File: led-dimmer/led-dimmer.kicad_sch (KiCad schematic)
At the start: 14 parts, among them J1 Screw_Terminal_01x02, J2 Screw_Terminal_01x02, Q1 IRLML6344, U1 LM555xM

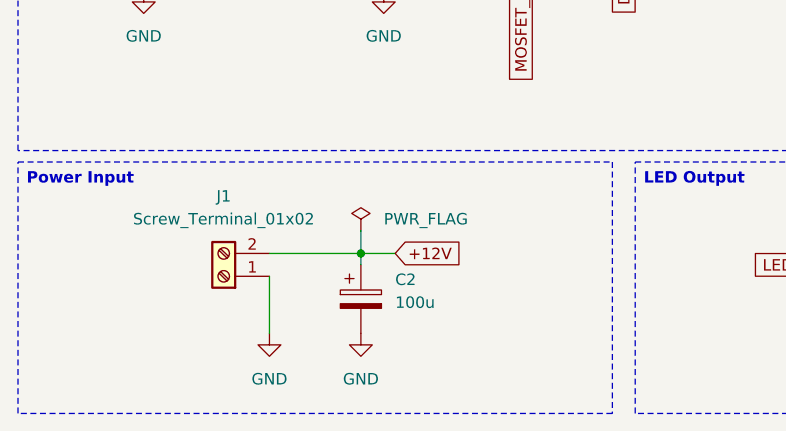
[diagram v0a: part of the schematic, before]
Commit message: Updated LED Schematic and PCB
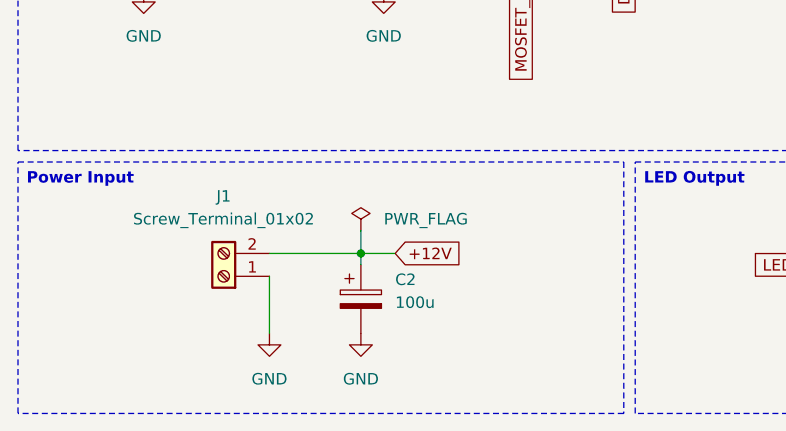
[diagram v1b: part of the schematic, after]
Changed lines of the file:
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@@
 	(title_block
 		(title "LED Dimmer Schematic")
-		(date "2026-06-28")
+		(date "2026-07-20")
 		(rev "1.0")
 	)
@@
 		(exclude_from_sim no)
 		(at 16.51 77.47 0)
-		(size 66.04 27.94)
+		(size 67.31 27.94)
 		(margins 0.9525 0.9525 0.9525 0.9525)
 		(stroke

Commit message: Updated output connectors and slimmed LED Dimmer PCB
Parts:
- removed J1, J2: Screw_Terminal_01x02, TerminalBlock:TerminalBlock_MaiXu_MX126-5.0-02P_1x02_P5.00mm, symbol Connector:Screw_Terminal_01x02
- added J1, J2: Conn_01x02_Pin, Connector_JST:JST_PH_B2B-PH-K_1x02_P2.00mm_Vertical, symbol Connector:Conn_01x02_Pin
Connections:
- net +12V: now also J1.1 (Pin_1), J2.1 (Pin_1)
- net GND: now also J1.2 (Pin_2)
- net LED_PWM: now also J2.2 (Pin_2)
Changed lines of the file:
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@@
 	(title_block
 		(title "LED Dimmer Schematic")
-		(date "2026-07-20")
+		(date "2026-07-25")
 		(rev "1.0")
 	)
@@
 				(path "/97f4d0d2-49dd-4867-ad6b-0ece5467e23e"
 					(reference "R2")
+					(unit 1)
+				)
+			)
+		)
+	)
+	(symbol
+		(lib_id "Connector:Conn_01x02_Pin")
+		(at 114.3 91.44 180)
+		(unit 1)
+		(body_style 1)
+		(exclude_from_sim no)
+		(in_bom yes)
+		(on_board yes)
+		(in_pos_files yes)
+		(dnp no)
+		(fields_autoplaced yes)
+		(property "Reference" "J2"
+			(at 115.57 88.8999 0)
+			(show_name no)
+			(do_not_autoplace no)
+			(effects
+				(font
+					(size 1.27 1.27)
+				)
+				(justify right)
+			)
+		)
+		(property "Value" "Conn_01x02_Pin"
+			(at 115.57 91.4399 0)
+			(show_name no)
+			(do_not_autoplace no)
+			(effects
+				(font
+					(size 1.27 1.27)
+				)
+				(justify right)
+			)
+		)
+		(property "Footprint" "Connector_JST:JST_PH_B2B-PH-K_1x02_P2.00mm_Vertical"
+			(at 114.3 91.44 0)
+			(hide yes)
+			(show_name no)
+			(do_not_autoplace no)
+			(effects
+				(font
+					(size 1.27 1.27)
+				)
+			)
+		)
+		(property "Datasheet" ""
+			(at 114.3 91.44 0)
+			(hide yes)
+			(show_name no)
+			(do_not_autoplace no)
+			(effects
+				(font
+					(size 1.27 1.27)
+				)
+			)
+		)
+		(property "Description" "Generic connector, single row, 01x02, script generated"
+			(at 114.3 91.44 0)
+			(hide yes)
+			(show_name no)
+			(do_not_autoplace no)
+			(effects
+				(font
+					(size 1.27 1.27)
+				)
+			)
+		)
+		(pin "1"
+		)
+		(pin "2"
+		)
+		(instances
+			(project "led-dimmer"
+				(path "/97f4d0d2-49dd-4867-ad6b-0ece5467e23e"
+					(reference "J2")
 					(unit 1)
 				)
@@
 				(path "/97f4d0d2-49dd-4867-ad6b-0ece5467e23e"
 					(reference "#PWR02")
-					(unit 1)
-				)
-			)
-		)
-	)
-	(symbol
-		(lib_id "Connector:Screw_Terminal_01x02")
-		(at 39.37 90.17 180)
-		(unit 1)
-		(body_style 1)
-		(exclude_from_sim no)
-		(in_bom yes)
-		(on_board yes)
-		(in_pos_files yes)
-		(dnp no)
-		(fields_autoplaced yes)
-		(property "Reference" "J1"
-			(at 39.37 81.28 0)
-			(show_name no)
-			(do_not_autoplace no)
-			(effects
-				(font
-					(size 1.27 1.27)
-				)
-			)
-		)
-		(property "Value" "Screw_Terminal_01x02"
-			(at 39.37 83.82 0)
-			(show_name no)
-			(do_not_autoplace no)
-			(effects
-				(font
-					(size 1.27 1.27)
-				)
-			)
-		)
-		(property "Footprint" "TerminalBlock:TerminalBlock_MaiXu_MX126-5.0-02P_1x02_P5.00mm"
-			(at 39.37 90.17 0)
-			(hide yes)
-			(show_name no)
-			(do_not_autoplace no)
-			(effects
-				(font
-					(size 1.27 1.27)
-				)
-			)
-		)
-		(property "Datasheet" ""
-			(at 39.37 90.17 0)
-			(hide yes)
-			(show_name no)
-			(do_not_autoplace no)
-			(effects
-				(font
-					(size 1.27 1.27)
-				)
-			)
-		)
-		(property "Description" "Generic screw terminal, single row, 01x02, script generated (kicad-library-utils/schlib/autogen/connector/)"
-			(at 39.37 90.17 0)
-			(hide yes)
-			(show_name no)
-			(do_not_autoplace no)
-			(effects
-				(font
-					(size 1.27 1.27)
-				)
-			)
-		)
-		(pin "1"
-		)
-		(pin "2"
-		)
-		(instances
-			(project "led-dimmer"
-				(path "/97f4d0d2-49dd-4867-ad6b-0ece5467e23e"
-					(reference "J1")
 					(unit 1)
 				)
@@
 	)
 	(symbol
-		(lib_id "Connector:Screw_Terminal_01x02")
-		(at 114.3 88.9 0)
-		(unit 1)
-		(body_style 1)
-		(exclude_from_sim no)
-		(in_bom yes)
-		(on_board yes)
-		(in_pos_files yes)
-		(dnp no)
-		(fields_autoplaced yes)
-		(property "Reference" "J2"
-			(at 116.84 88.8999 0)
-			(show_name no)
-			(do_not_autoplace no)
-			(effects
-				(font
-					(size 1.27 1.27)
-				)
-				(justify left)
-			)
-		)
-		(property "Value" "Screw_Terminal_01x02"
-			(at 116.84 91.4399 0)
-			(show_name no)
-			(do_not_autoplace no)
-			(effects
-				(font
-					(size 1.27 1.27)
-				)
-				(justify left)
-			)
-		)
-		(property "Footprint" "TerminalBlock:TerminalBlock_MaiXu_MX126-5.0-02P_1x02_P5.00mm"
-			(at 114.3 88.9 0)
-			(hide yes)
-			(show_name no)
-			(do_not_autoplace no)
-			(effects
-				(font
-					(size 1.27 1.27)
-				)
-			)
-		)
-		(property "Datasheet" ""
-			(at 114.3 88.9 0)
-			(hide yes)
-			(show_name no)
-			(do_not_autoplace no)
-			(effects
-				(font
-					(size 1.27 1.27)
-				)
-			)
-		)
-		(property "Description" "Generic screw terminal, single row, 01x02, script generated (kicad-library-utils/schlib/autogen/connector/)"
-			(at 114.3 88.9 0)
-			(hide yes)
-			(show_name no)
-			(do_not_autoplace no)
-			(effects
-				(font
-					(size 1.27 1.27)
-				)
-			)
-		)
-		(pin "1"
-		)
-		(pin "2"
-		)
-		(instances
-			(project "led-dimmer"
-				(path "/97f4d0d2-49dd-4867-ad6b-0ece5467e23e"
-					(reference "J2")
-					(unit 1)
-				)
-			)
-		)
-	)
-	(symbol
 		(lib_id "Device:C")
 		(at 48.26 33.02 90)
@@
 					(unit 1)
 				)
+			)
+		)
+	)
+	(symbol
+		(lib_id "Connector:Conn_01x02_Pin")
+		(at 39.37 87.63 0)
+		(unit 1)
+		(body_style 1)
+		(exclude_from_sim no)
+		(in_bom yes)
+		(on_board yes)
+		(in_pos_files yes)
+		(dnp no)
+		(fields_autoplaced yes)
+		(property "Reference" "J1"
+			(at 40.005 82.55 0)
+			(show_name no)
+			(do_not_autoplace no)
+			(effects
+				(font
+					(size 1.27 1.27)
+				)
+			)
+		)
+		(property "Value" "Conn_01x02_Pin"
+			(at 40.005 85.09 0)
+			(show_name no)
+			(do_not_autoplace no)
+			(effects
+				(font
+					(size 1.27 1.27)
+				)
+			)
+		)
+		(property "Footprint" "Connector_JST:JST_PH_B2B-PH-K_1x02_P2.00mm_Vertical"
+			(at 39.37 87.63 0)
+			(hide yes)
+			(show_name no)
+			(do_not_autoplace no)
+			(effects
+				(font
+					(size 1.27 1.27)
+				)
+			)
+		)
+		(property "Datasheet" ""
+			(at 39.37 87.63 0)
+			(hide yes)
+			(show_name no)
+			(do_not_autoplace no)
+			(effects
+				(font
+					(size 1.27 1.27)
+				)
+			)
+		)
+		(property "Description" "Generic connector, single row, 01x02, script generated"
+			(at 39.37 87.63 0)
+			(hide yes)
+			(show_name no)
+			(do_not_autoplace no)
+			(effects
+				(font
+					(size 1.27 1.27)
+				)
+			)
+		)
+		(pin "1"
+		)
+		(pin "2"
+		)
+		(instances
+			(project "led-dimmer"
+				(path "/97f4d0d2-49dd-4867-ad6b-0ece5467e23e"
+					(reference "J1")
+					(unit 1)
+				)

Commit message: Update LED dimmer PCB for revised components
- Switch power and LED connections to JST B2B-XH-A connectors
- Update bulk capacitor to 470uF
- Change NE555 to DIP-8 package
- Increase PCB size and revise component placement/routing
- Update schematic reference designators
- Refresh README component and design documentation
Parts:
- removed U1: LM555xM, Package_SO:SOIC-8_3.9x4.9mm_P1.27mm, symbol Timer:LM555xM
- added U1: NE555P, Package_DIP:DIP-8_W7.62mm, symbol Timer:NE555P
- C3: renamed from C2; value 100u -> 470u; footprint Capacitor_THT:CP_Radial_D5.0mm_P2.50mm -> Capacitor_THT:CP_Radial_D6.3mm_P2.50mm
- J1, J2: footprint Connector_JST:JST_PH_B2B-PH-K_1x02_P2.00mm_Vertical -> footprints:JST_B2B-XH-A
- renumbered C3 to C2
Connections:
- net +12V: now also U1.4 (~{RST}), U1.8 (VCC)
- net DISCHARGE: now also U1.7 (DISCH)
- net GND: now also U1.1 (GND)
- net TIMING: now also U1.2 (TRIG), U1.6 (THRES)
- net at R2.2: now also U1.3 (OUT)
- net at C2.2: now also U1.5 (CONT)
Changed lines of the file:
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@@
 	(title_block
 		(title "LED Dimmer Schematic")
-		(date "2026-07-25")
-		(rev "1.0")
+		(date "2026-08-15")
+		(rev "1.1")
 	)
 	(text_box "Power Input"
@@
 	)
 	(junction
-		(at 57.15 55.88)
-		(diameter 0)
-		(color 0 0 0 0)
-	)
-	(junction
 		(at 124.46 44.45)
 		(diameter 0)
@@
 	(junction
 		(at 35.56 43.18)
+		(diameter 0)
+		(color 0 0 0 0)
+	)
+	(junction
+		(at 57.15 55.88)
 		(diameter 0)
 		(color 0 0 0 0)
@@
 			)
 		)
-		(property "Footprint" "Connector_JST:JST_PH_B2B-PH-K_1x02_P2.00mm_Vertical"
+		(property "Footprint" "footprints:JST_B2B-XH-A"
 			(at 114.3 91.44 0)
 			(hide yes)
@@
 		(in_pos_files yes)
 		(dnp no)
-		(property "Reference" "C2"
+		(property "Reference" "C3"
 			(at 58.42 90.5509 0)
 			(show_name no)
@@
 			)
 		)
-		(property "Value" "100u"
+		(property "Value" "470u"
 			(at 58.42 93.0909 0)
 			(show_name no)
@@
 			)
 		)
-		(property "Footprint" "Capacitor_THT:CP_Radial_D5.0mm_P2.50mm"
+		(property "Footprint" "Capacitor_THT:CP_Radial_D6.3mm_P2.50mm"
 			(at 55.5752 96.52 0)
 			(hide yes)
@@
 			(project "led-dimmer"
 				(path "/97f4d0d2-49dd-4867-ad6b-0ece5467e23e"
-					(reference "C2")
+					(reference "C3")
 					(unit 1)
 				)
@@
 		(dnp no)
 		(fields_autoplaced yes)
-		(property "Reference" "#PWR04"
+		(property "Reference" "#PWR03"
 			(at 44.45 102.87 0)
 			(hide yes)
@@
 			(project "led-dimmer"
 				(path "/97f4d0d2-49dd-4867-ad6b-0ece5467e23e"
-					(reference "#PWR04")
+					(reference "#PWR03")
 					(unit 1)
 				)
@@
 		(dnp no)
 		(fields_autoplaced yes)
-		(property "Reference" "#PWR02"
+		(property "Reference" "#PWR04"
 			(at 54.61 102.87 0)
 			(hide yes)
@@
 			(project "led-dimmer"
 				(path "/97f4d0d2-49dd-4867-ad6b-0ece5467e23e"
-					(reference "#PWR02")
+					(reference "#PWR04")
 					(unit 1)
 				)
@@
 		(dnp no)
 		(fields_autoplaced yes)
-		(property "Reference" "#PWR03"
+		(property "Reference" "#PWR02"
 			(at 40.64 41.91 0)
 			(hide yes)
@@
 			(project "led-dimmer"
 				(path "/97f4d0d2-49dd-4867-ad6b-0ece5467e23e"
-					(reference "#PWR03")
+					(reference "#PWR02")
 					(unit 1)
 				)
@@
 	)
 	(symbol
-		(lib_name "LM555xM_1")
-		(lib_id "Timer:LM555xM")
+		(lib_id "Timer:NE555P")
 		(at 57.15 45.72 0)
 		(unit 1)
@@
 		(in_pos_files yes)
 		(dnp no)
+		(fields_autoplaced yes)
 		(property "Reference" "U1"
-			(at 64.77 34.29 0)
-			(show_name no)
-			(do_not_autoplace no)
-			(effects
-				(font
-					(size 1.27 1.27)
-				)
-			)
-		)
-		(property "Value" "LM555xM"
-			(at 64.77 36.83 0)
-			(show_name no)
-			(do_not_autoplace no)
-			(effects
-				(font
-					(size 1.27 1.27)
-				)
-			)
-		)
-		(property "Footprint" "Package_SO:SOIC-8_3.9x4.9mm_P1.27mm"
+			(at 69.85 39.2998 0)
+			(show_name no)
+			(do_not_autoplace no)
+			(effects
+				(font
+					(size 1.27 1.27)
+				)
+			)
+		)
+		(property "Value" "NE555P"
+			(at 69.85 41.8398 0)
+			(show_name no)
+			(do_not_autoplace no)
+			(effects
+				(font
+					(size 1.27 1.27)
+				)
+			)
+		)
+		(property "Footprint" "Package_DIP:DIP-8_W7.62mm"
 			(at 57.15 69.85 0)
 			(hide yes)
@@
 			)
 		)
-		(property "Datasheet" "http://www.ti.com/lit/ds/symlink/lm555.pdf"
+		(property "Datasheet" "http://www.ti.com/lit/ds/symlink/ne555.pdf"
 			(at 57.15 72.39 0)
 			(hide yes)
@@
 			)
 		)
-		(property "Description" "Timer, 555 compatible, SOIC-8"
+		(property "Description" "Precision Timers, 555 compatible, PDIP-8"
 			(at 57.15 67.31 0)
 			(hide yes)
@@
 			)
 		)
+		(pin "8"
+		)
+		(pin "4"
+		)
+		(pin "5"
+		)
 		(pin "6"
 		)
-		(pin "5"
+		(pin "1"
 		)
 		(pin "7"
 		)
+		(pin "2"
+		)
 		(pin "3"
-		)
-		(pin "2"
-		)
-		(pin "1"
-		)
-		(pin "4"
-		)
-		(pin "8"
 		)
 		(instances
@@
 		(dnp no)
 		(fields_autoplaced yes)
-		(property "Reference" "C3"
+		(property "Reference" "C2"
 			(at 48.26 25.4 90)
 			(show_name no)
@@
 			(project "led-dimmer"
 				(path "/97f4d0d2-49dd-4867-ad6b-0ece5467e23e"
-					(reference "C3")
+					(reference "C2")
 					(unit 1)
 				)
@@
 			)
 		)
-		(property "Footprint" "Connector_JST:JST_PH_B2B-PH-K_1x02_P2.00mm_Vertical"
+		(property "Footprint" "footprints:JST_B2B-XH-A"
 			(at 39.37 87.63 0)
 			(hide yes)

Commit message: Fixed diode direction on led-dimmer PCB
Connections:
- net DISCHARGE: now also D1.1 (K), D2.2 (A); no longer D1.2 (A), D2.1 (K)
- net at R3.3: now also D1.2 (A); no longer D1.1 (K)
- net at R3.1: now also D2.1 (K); no longer D2.2 (A)
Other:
- moved on the sheet: D1, D2
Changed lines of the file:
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@@
 	(title_block
 		(title "LED Dimmer Schematic")
-		(date "2026-09-09")
-		(rev "1.2")
+		(date "2026-10-01")
+		(rev "1.3")
 	)
 	(text_box "Power Input"
@@
 	(symbol
 		(lib_id "Diode:1N4148W")
-		(at 87.63 44.45 180)
+		(at 87.63 44.45 0)
 		(unit 1)
 		(body_style 1)
@@
 		)
 		(property "Footprint" "Diode_SMD:D_SOD-123"
-			(at 87.63 40.005 0)
+			(at 87.63 48.895 0)
 			(hide yes)
 			(show_name no)
@@
 	(symbol
 		(lib_id "Diode:1N4148W")
-		(at 110.49 44.45 180)
+		(at 110.49 44.45 0)
 		(unit 1)
 		(body_style 1)
@@
 		(dnp no)
 		(property "Reference" "D2"
-			(at 110.49 38.1 0)
+			(at 110.49 50.8 0)
 			(show_name no)
 			(do_not_autoplace no)
@@
 		)
 		(property "Value" "1N4148W"
-			(at 110.49 40.64 0)
+			(at 110.49 48.26 0)
 			(show_name no)
 			(do_not_autoplace no)
@@
 		)
 		(property "Footprint" "Diode_SMD:D_SOD-123"
-			(at 110.49 40.005 0)
-			(hide yes)
-			(show_name no)
+			(at 110.49 48.895 0)
+			(hide yes)
+			(show_name no)
